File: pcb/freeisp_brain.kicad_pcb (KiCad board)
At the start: 2 copper layers, 100 x 100 mm, 26 parts, among them J1 12V IN, J10 BUZZER, J11 HORN, J12 SENSE, J2 5V AUX, J3 BATT, J4 TFT, J5 RC522, J7 REED, J8 LED R, J9 LED G, K1 HORN RLY, U1 LM2596 BUCK, U2 TP4056, U3A ESP32 L, U3B ESP32 R, U4 MPU-6050

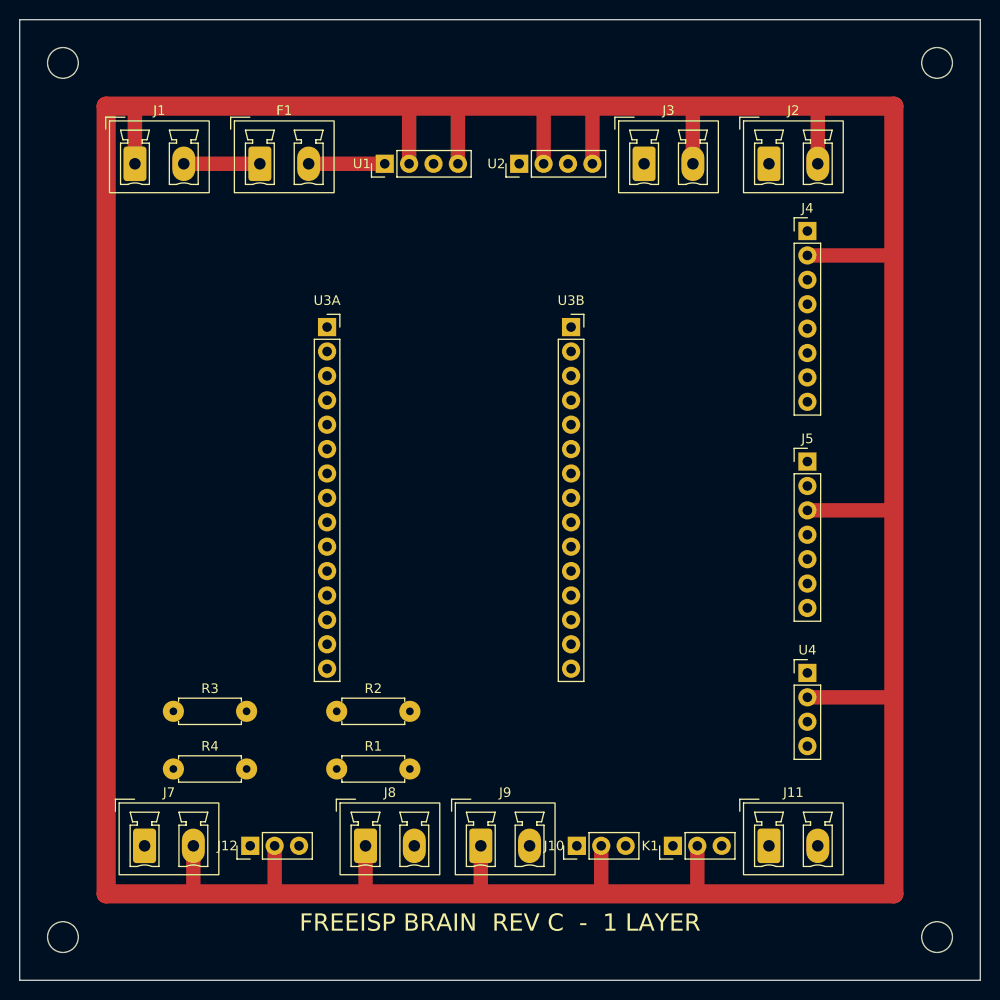
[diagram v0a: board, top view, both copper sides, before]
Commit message: Route the brain board: 0 DRC errors, 0 unconnected
router.py is a grid maze router with real clearance inflation - every
obstacle is grown by (my_half + clearance + their_half) and any cell whose
centre falls inside is blocked, so KiCad's DRC agrees with it.

It routes F.Cu first and falls back to a wire link where the single layer
genuinely cannot get through. Three orderings are tried (power-first,
shortest-first, longest-first) and whichever needs fewest links wins;
shortest-first currently wins at 19 links and 190 etched segments.

B.Cu is never etched - tracks there are insulated wires soldered across the
component side. Because such wires cross freely, links are not obstacles to
each other and a .kicad_dru rule sets B.Cu-to-B.Cu clearance to zero. They
still clear every pad so a nicked wire cannot short onto one.

Two bugs the DRC caught and fixed:
- unused ESP32 pins (TX0, RX0, GPIO15) were not obstacles, so four traces
  ran straight across them. An unconnected pad is still copper.
- forcing links to clear each other made 12 nets unroutable; that constraint
  was modelling etched copper, not wire.

19 links is high. Cutting it means flipping J4/J5/U4 (free) or reassigning
the freely-chosen GPIOs to match header order (needs firmware pin changes).

Co-Authored-By: Claude Opus 5 (1M context) <noreply@anthropic.com>
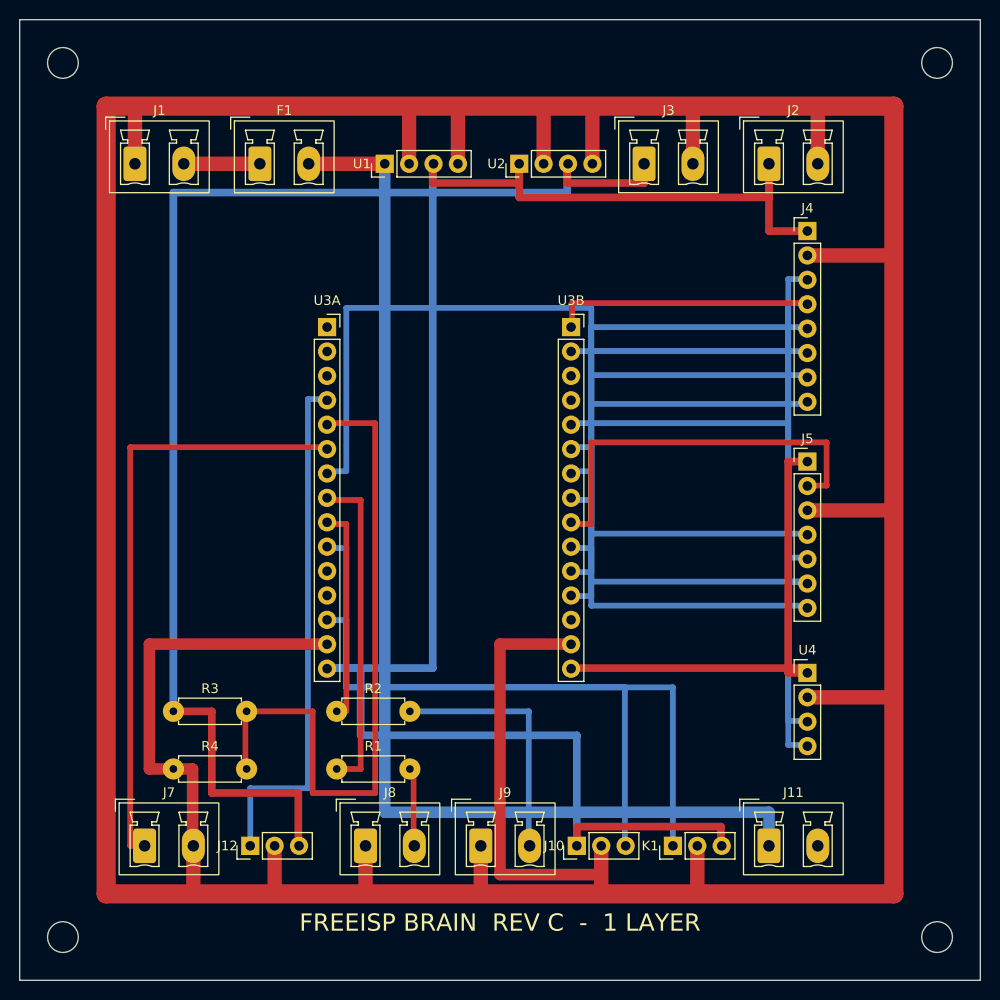
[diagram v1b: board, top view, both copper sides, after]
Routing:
- net +5V: track 0.00 -> 184.0 mm
- net VBAT: track 0.00 -> 137.0 mm
- net +12V: track 7.92 -> 118.9 mm
- net GND: track 427.0 -> 515.9 mm
- net TFT_BLK: track 0.00 -> 77.1 mm
- net SCK: track 0.00 -> 71.7 mm
- net SENSE_BATT: track 0.00 -> 71.4 mm
- net SCL: track 0.00 -> 65.6 mm
- net REED: track 0.00 -> 63.5 mm
- net BUZZ: track 0.00 -> 62.0 mm
- net HORN_IN: track 0.00 -> 59.5 mm
- net MOSI: track 0.00 -> 57.6 mm
- net SDA: track 0.00 -> 55.6 mm
- net SENSE_MAINS: track 0.00 -> 54.5 mm
- net +3V3: track 0.00 -> 51.1 mm
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
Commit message: Two layers: 0 errors, 0 unconnected, 17 vias, no wire links
Francis chose two layers - same price at PCBWay and it removes the 19 hand
soldered wires entirely. The router now searches (cell, layer, heading) with
a via penalty, so a path can change layer mid-route instead of being stuck on
one side. Through-hole pads already join the layers, so a path may start and
end on either without a via.

Real footprint errors found and fixed - DRC checks geometry, not whether a
footprint matches a part, so all of these passed clean before:
- J5 RC522 had 7 pins. The module has 8; IRQ is unused but still has a leg.
- U4 MPU-6050 had 4 pins. The GY-521 has 8.
- J4 TFT had VCC and GND swapped against the module's own silkscreen order
  (GND VDD SCL SDA RST DC CS BLK).

The LM2596 and TP4056 are wire-pad modules, not pluggable headers - his photo
of the TP4056 settled it. They now bolt alongside and land on 4-way screw
terminals, which removes two footprints that could not be verified. The 12V
feed is fused inline in the wire, so F1, J2 and J3 are gone.

Design rules moved from etching to fab values: 0.25mm clearance, 0.4mm
tracks, library pad sizes.

fitcheck_1to1.pdf plots at exact scale - print it, sit the real parts on it,
confirm every pin lands on its hole. Nothing gets ordered until that passes.

Still open: backup power. The TP4056 outputs 3.0-4.2V with no switchover, so
running off the 18650 needs a boost that is not on this board.

Co-Authored-By: Claude Opus 5 (1M context) <noreply@anthropic.com>
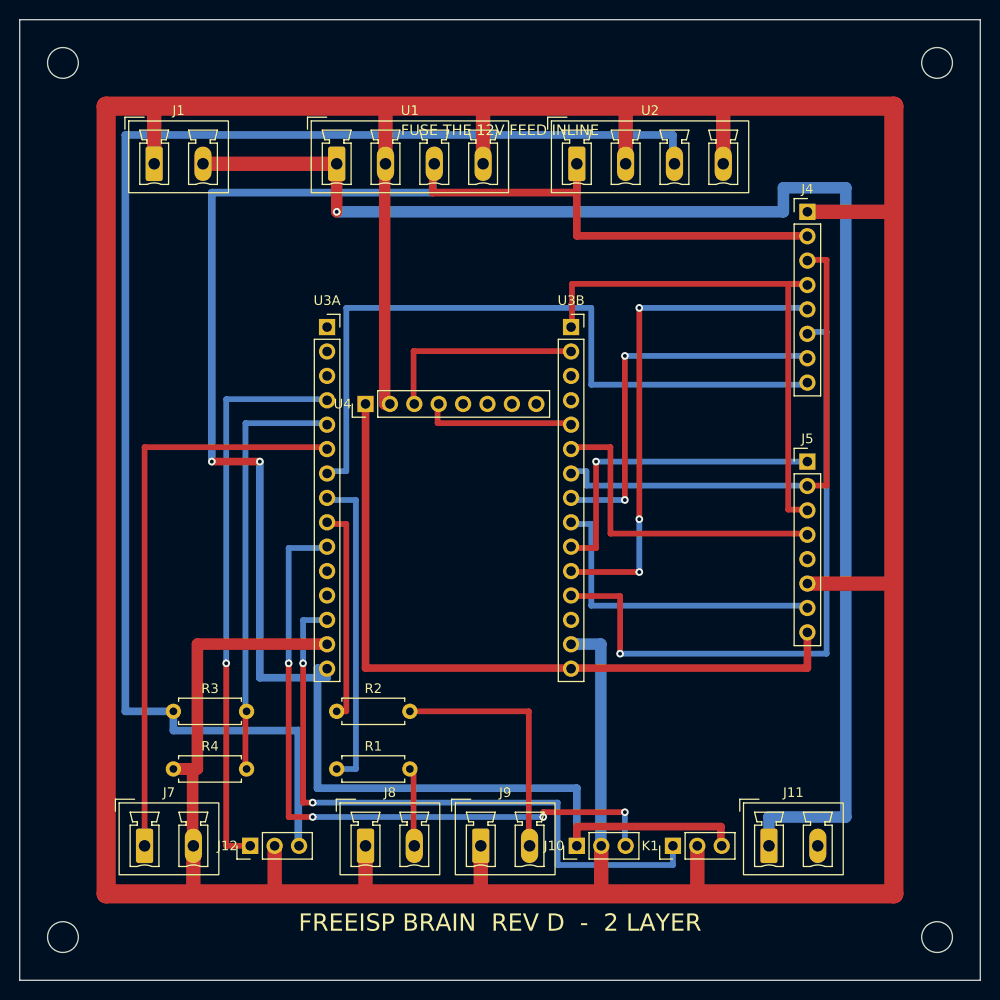
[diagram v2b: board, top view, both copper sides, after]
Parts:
- removed F1: FUSE 2A, Connector_Phoenix_MC_HighVoltage:PhoenixContact_MCV_1,5_2-G-5.08_1x02_P5.08mm_Vertical
- removed J2: 5V AUX, Connector_Phoenix_MC_HighVoltage:PhoenixContact_MCV_1,5_2-G-5.08_1x02_P5.08mm_Vertical
- removed J3: BATT, Connector_Phoenix_MC_HighVoltage:PhoenixContact_MCV_1,5_2-G-5.08_1x02_P5.08mm_Vertical
- J5: footprint Connector_PinHeader_2.54mm:PinHeader_1x07_P2.54mm_Vertical -> Connector_PinHeader_2.54mm:PinHeader_1x08_P2.54mm_Vertical
- U1: value LM2596 BUCK -> BUCK IN+ IN- OUT+ OUT-; footprint Connector_PinHeader_2.54mm:PinHeader_1x04_P2.54mm_Vertical -> Connector_Phoenix_MC_HighVoltage:PhoenixContact_MCV_1,5_4-G-5.08_1x04_P5.08mm_Vertical
- U2: value TP4056 -> CHARGER IN+ IN- B+ B-; footprint Connector_PinHeader_2.54mm:PinHeader_1x04_P2.54mm_Vertical -> Connector_Phoenix_MC_HighVoltage:PhoenixContact_MCV_1,5_4-G-5.08_1x04_P5.08mm_Vertical
- U4: footprint Connector_PinHeader_2.54mm:PinHeader_1x04_P2.54mm_Vertical -> Connector_PinHeader_2.54mm:PinHeader_1x08_P2.54mm_Vertical
- moved U4 53.9 mm to (96.0, 80.0), turned to 90 degrees
- moved U2 6.00 mm to (118.0, 55.0), turned to 0 degrees
- moved U1 5.00 mm to (93.0, 55.0), turned to 0 degrees
- moved J1 2.00 mm to (74.0, 55.0)
- moved J4 2.00 mm to (142.0, 60.0)
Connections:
- J1 pad 2: +12V_RAW -> +12V
- J4 pad 1: +5V -> GND
- J4 pad 2: GND -> +5V
- J5 pad 1: +3V3 -> RC_SS
- J5 pad 2: RC_RST -> SCK
- J5 pad 3: GND -> MOSI
- J5 pad 5: MOSI -> (no net)
- J5 pad 6: SCK -> GND
- J5 pad 7: RC_SS -> RC_RST
- U4 pad 3: SDA -> SCL
- U4 pad 4: SCL -> SDA
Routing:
- net SCL: track 65.6 -> 21.9 mm
- net SDA: track 55.6 -> 15.9 mm
- net +12V: track 118.9 -> 150.9 mm, vias 0 -> 1
- net SENSE_BATT: track 71.4 -> 44.6 mm
- net +3V3: track 51.1 -> 77.2 mm
- net +5V: track 184.0 -> 207.5 mm, vias 0 -> 2
- net GND: track 515.9 -> 494.7 mm
- net SCK: track 71.7 -> 53.7 mm
- net TFT_DC: track 50.1 -> 68.1 mm, vias 0 -> 1
- net VBAT: track 137.0 -> 152.0 mm
- net HORN_IN: track 59.5 -> 68.5 mm, vias 0 -> 2
- net BUZZ: track 62.0 -> 71.0 mm, vias 0 -> 4
- net RC_RST: track 41.6 -> 33.2 mm
- net +12V_RAW: track 7.92 -> 0.00 mm
- net SENSE_MAINS: track 54.5 -> 59.5 mm, vias 0 -> 1
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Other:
- board text added: "FREEISP BRAIN REV D - 2 LAYER"
- board text added: "FUSE THE 12V FEED INLINE"
- board text removed: "FREEISP BRAIN REV C - 1 LAYER"

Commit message: Backup power on the board: boost terminal + 1N5822 diode-OR, rev D
Francis asked for the step-down, the step-up and the diodes that join them
all accounted for on the board. Done:

- J13 BOOST terminal (IN+ IN- OUT+ OUT-): battery -> 5V step-up module,
  bolted alongside like the buck and charger.
- D1/D2 1N5822 Schottky diode-OR where the two 5V rails meet. Mains alive:
  buck wins through D1. Mains cut: boost takes over through D2. The
  changeover is physics, not code.
- New 5V_SYS net after the diodes feeds ESP32 VIN, TFT, buzzer and horn
  relay - everything that must keep working when a thief cuts the power.
- Charger IN+ deliberately stays on the buck rail: fed from 5V_SYS the
  battery would charge itself through the boost.

Also moved U4 (MPU header) out of the channel between the ESP32 socket rows
- the channel is a dead end, every trace had to come the long way round and
six nets knotted around it (the mess Francis circled). All three peripheral
headers now stack down the right edge.

0 DRC errors, 0 unconnected, 12 vias.

Co-Authored-By: Claude Opus 5 (1M context) <noreply@anthropic.com>
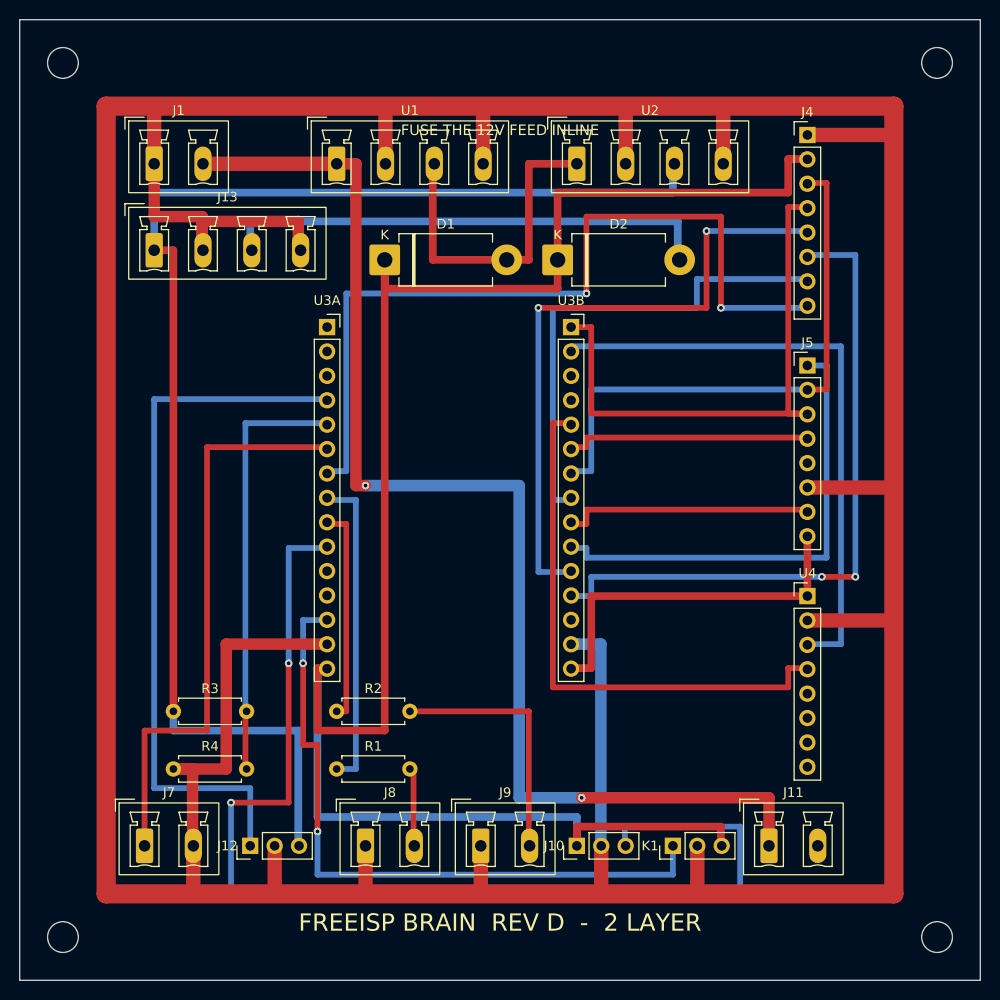
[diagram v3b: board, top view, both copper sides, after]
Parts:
- added D1: 1N5822, Diode_THT:D_DO-201AD_P12.70mm_Horizontal, F.Cu at (98.0, 65.0)
- added D2: 1N5822, Diode_THT:D_DO-201AD_P12.70mm_Horizontal, F.Cu at (116.0, 65.0)
- added J13: BOOST IN+ IN- OUT+ OUT-, Connector_Phoenix_MC_HighVoltage:PhoenixContact_MCV_1,5_4-G-5.08_1x04_P5.08mm_Vertical, F.Cu at (74.0, 64.0)
- moved U4 50.2 mm to (142.0, 100.0), turned to 0 degrees
- moved J5 10.0 mm to (142.0, 76.0)
- moved J4 8.00 mm to (142.0, 52.0)
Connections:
- J10 pad 1: +5V -> +5V_SYS
- J4 pad 2: +5V -> +5V_SYS
- K1 pad 3: +5V -> +5V_SYS
- U3A pad 15: +5V -> +5V_SYS
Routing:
- net +5V_SYS: track 0.00 -> 189.5 mm
- net +5V: track 207.5 -> 35.0 mm, vias 2 -> 0
- net +5V_BAT: track 0.00 -> 51.6 mm
- net BUZZ: track 71.0 -> 119.0 mm, vias 4 -> 2
- net SDA: track 15.9 -> 57.9 mm
- net SCL: track 21.9 -> 63.1 mm
- net +3V3: track 77.2 -> 38.3 mm
- net +12V: track 150.9 -> 129.9 mm, vias 1 -> 2
- net RC_SS: track 33.6 -> 49.6 mm, vias 1 -> 0
- net SENSE_MAINS: track 59.5 -> 74.5 mm, vias 1 -> 0
- net TFT_RST: track 52.1 -> 66.9 mm, vias 3 -> 2
- net GND: track 494.7 -> 508.2 mm
- net VBAT: track 152.0 -> 140.0 mm
- net TFT_CS: track 39.7 -> 51.5 mm, vias 2 -> 0
- net TFT_BLK: track 75.1 -> 86.1 mm, vias 0 -> 2
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
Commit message: Triple-verified sweep: audit.py + DRC + renders, every pin named on silk
Francis asked for a full sweep with everything confirmed three times and
every pin named so he can verify. Three independent checks, all passing:

1. audit.py (NEW) - parses the board file KiCad reads, not the generator's
   own data, so a generator bug cannot hide itself. Checks every pair of
   different-net copper for crossings/clearance ("wires intermarrying") and
   that every net's pads form one connected island. CLEAN on both.
2. kicad-cli DRC: 0 errors, 0 unconnected.
3. Front + back renders inspected; pin map cross-checked against the bench-
   proven firmware defines (all 16 pins match LiveDashboardNext/CardDisarm).

Every connector pin is now NAMED ON THE SILKSCREEN using the names printed
on the module it wires to (TFT: GND VDD SCL SDA RST DC CS BLK, etc), plus
ESP32 orientation marks (EN/VIN/D23/3V3 corners, ANTENNA SIDE / USB SIDE).
PINOUT.md is the printed confirmation sheet for the paper test.

Silk cleanup driven by DRC: boost terminal turned vertical down the left
edge (its labels sat on its own body art), bottom labels moved off the
measured terminal outline (silk reaches 4.85mm above the pad row), three
reference texts relocated, refs hidden on the three tight bottom headers in
favour of SENSE/BUZZ/RELAY headings. silk_overlap 49 -> 0.

Co-Authored-By: Claude Opus 5 (1M context) <noreply@anthropic.com>
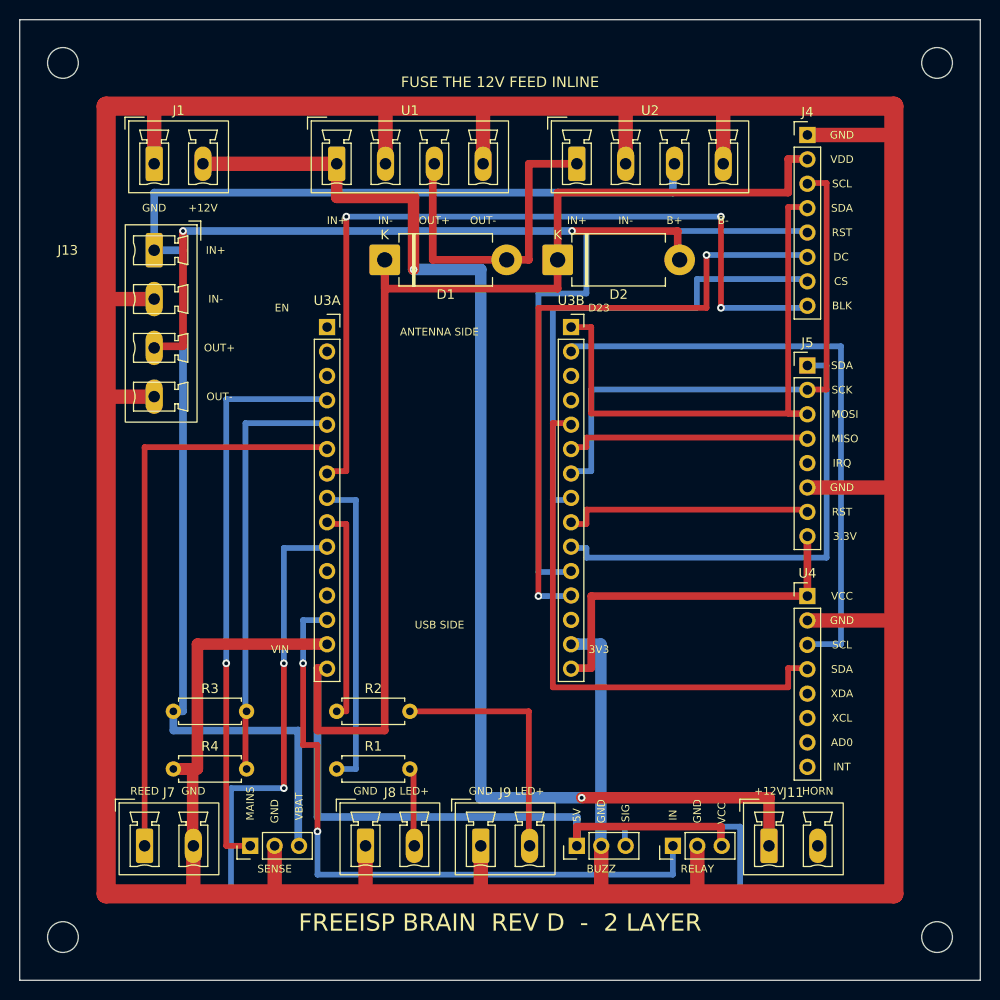
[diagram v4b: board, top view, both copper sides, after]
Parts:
- turned J13 to 270 degrees
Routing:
- net GND: track 508.2 -> 488.1 mm
- net +5V_BAT: track 51.6 -> 69.6 mm, vias 0 -> 2
- net SENSE_MAINS: track 74.5 -> 59.5 mm, vias 0 -> 1
- net TFT_DC: track 70.1 -> 66.9 mm
- net VBAT: track 140.0 -> 142.0 mm
- net TFT_RST: vias 2 -> 0
- net TFT_BLK: vias 2 -> 3
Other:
- board text added: "+12V"
- board text added: "3.3V"
- board text added: "3V3"
- board text added: "5V"
- board text added: "AD0"
- board text added: "ANTENNA SIDE"
- board text added: "B+"
- board text added: "B-"
- board text added: "BLK"
- board text added: "BUZZ"
- board text added: "CS"
- board text added: "D23"
- board text added: "DC"
- board text added: "EN"
- board text added: "GND"
- board text added: "HORN"
- board text added: "IN"
- board text added: "IN+"
- board text added: "IN-"
- board text added: "INT"
- board text added: "IRQ"
- board text added: "LED+"
- board text added: "MAINS"
- board text added: "MISO"
- board text added: "MOSI"
- board text added: "OUT+"
- board text added: "OUT-"
- board text added: "REED"
- board text added: "RELAY"
- board text added: "RST"
- board text added: "SCK"
- board text added: "SCL"
- board text added: "SDA"
- board text added: "SENSE"
- board text added: "SIG"
- board text added: "USB SIDE"
- board text added: "VBAT"
- board text added: "VCC"
- board text added: "VDD"
- board text added: "VIN"
- board text added: "XCL"
- board text added: "XDA"
